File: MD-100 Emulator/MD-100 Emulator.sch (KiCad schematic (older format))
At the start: 12 parts

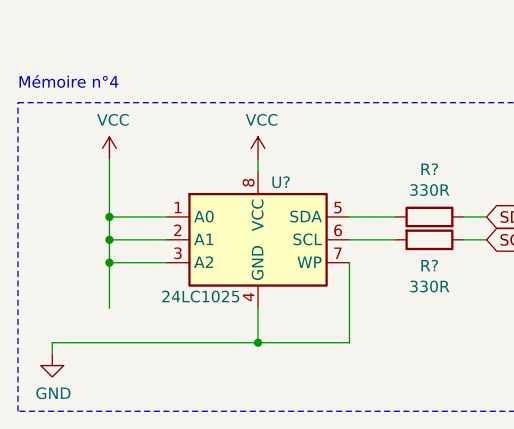
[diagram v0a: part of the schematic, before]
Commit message: j'ai enlevé un bout de ficelle qui gênait
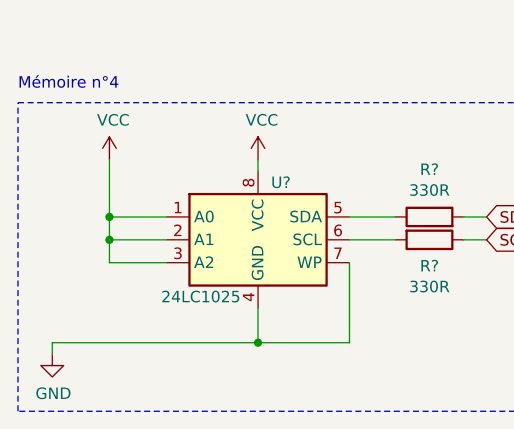
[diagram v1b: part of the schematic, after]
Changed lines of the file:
@@
 Wire Wire Line
 	1250 6800 1000 6800
-Connection ~ 1000 6800
-Wire Wire Line
-	1000 6800 1000 7000
 Wire Wire Line
 	1250 6700 1000 6700

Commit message: cours pcb alexx08
merci max de me le rappeller
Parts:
- added J?: CPB_Connector, symbol CoursPCB:CPB_Connector
- added U? (x5): 74HC00, symbol 74xx:74HC00
- added U? (x5): 74HC02, symbol 74xx:74HC02
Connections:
- wire segments 64 -> 103
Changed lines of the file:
@@
 Wire Wire Line
 	1250 1200 1000 1200
+$Comp
+L 74xx:74HC00 U?
+U 1 1 5EBDC272
+P 5000 4200
+F 0 "U?" H 5000 3883 50  0000 C CNN
+F 1 "74HC00" H 5000 3974 50  0000 C CNN
+F 2 "" H 5000 4200 50  0001 C CNN
+F 3 "http://www.ti.com/lit/gpn/sn74hc00" H 5000 4200 50  0001 C CNN
+	1    5000 4200
+	-1   0    0    1
+$EndComp
+$Comp
+L 74xx:74HC00 U?
+U 2 1 5EBE2FB7
+P 5000 5350
+F 0 "U?" H 5000 5033 50  0000 C CNN
+F 1 "74HC00" H 5000 5124 50  0000 C CNN
+F 2 "" H 5000 5350 50  0001 C CNN
+F 3 "http://www.ti.com/lit/gpn/sn74hc00" H 5000 5350 50  0001 C CNN
+	2    5000 5350
+	-1   0    0    1
+$EndComp
+$Comp
+L 74xx:74HC00 U?
+U 3 1 5EBE8E3D
+P 5750 5650
+F 0 "U?" H 5750 5333 50  0000 C CNN
+F 1 "74HC00" H 5750 5424 50  0000 C CNN
+F 2 "" H 5750 5650 50  0001 C CNN
+F 3 "http://www.ti.com/lit/gpn/sn74hc00" H 5750 5650 50  0001 C CNN
+	3    5750 5650
+	-1   0    0    1
+$EndComp
+$Comp
+L 74xx:74HC00 U?
+U 4 1 5EBEC491
+P 6550 5650
+F 0 "U?" H 6550 5333 50  0000 C CNN
+F 1 "74HC00" H 6550 5424 50  0000 C CNN
+F 2 "" H 6550 5650 50  0001 C CNN
+F 3 "http://www.ti.com/lit/gpn/sn74hc00" H 6550 5650 50  0001 C CNN
+	4    6550 5650
+	-1   0    0    1
+$EndComp
+$Comp
+L 74xx:74HC00 U?
+U 5 1 5EBEE381
+P 3700 6800
+F 0 "U?" H 3930 6846 50  0000 L CNN
+F 1 "74HC00" H 3930 6755 50  0000 L CNN
+F 2 "" H 3700 6800 50  0001 C CNN
+F 3 "http://www.ti.com/lit/gpn/sn74hc00" H 3700 6800 50  0001 C CNN
+	5    3700 6800
+	1    0    0    -1
+$EndComp
+Wire Wire Line
+	5300 5450 5400 5450
+Wire Wire Line
+	5400 5450 5400 5650
+Wire Wire Line
+	5400 5650 5450 5650
+Wire Wire Line
+	6050 5550 6150 5550
+Wire Wire Line
+	6050 5750 6150 5750
+Wire Wire Line
+	6150 5550 6150 5650
+Wire Wire Line
+	6150 5650 6250 5650
+Connection ~ 6150 5650
+Wire Wire Line
+	6150 5650 6150 5750
+Wire Wire Line
+	4700 5350 4400 5350
+Wire Wire Line
+	4400 5350 4400 4450
+Wire Wire Line
+	4700 4200 4400 4200
+$Comp
+L 74xx:74HC02 U?
+U 2 1 5EC153C3
+P 5750 3950
+F 0 "U?" H 5750 3633 50  0000 C CNN
+F 1 "74HC02" H 5750 3724 50  0000 C CNN
+F 2 "" H 5750 3950 50  0001 C CNN
+F 3 "http://www.ti.com/lit/gpn/sn74hc02" H 5750 3950 50  0001 C CNN
+	2    5750 3950
+	-1   0    0    1
+$EndComp
+$Comp
+L 74xx:74HC02 U?
+U 1 1 5EC1C40E
+P 5750 4500
+F 0 "U?" H 5750 4183 50  0000 C CNN
+F 1 "74HC02" H 5750 4274 50  0000 C CNN
+F 2 "" H 5750 4500 50  0001 C CNN
+F 3 "http://www.ti.com/lit/gpn/sn74hc02" H 5750 4500 50  0001 C CNN
+	1    5750 4500
+	-1   0    0    1
+$EndComp
+$Comp
+L 74xx:74HC02 U?
+U 4 1 5EC20EBA
+P 5750 5050
+F 0 "U?" H 5750 4733 50  0000 C CNN
+F 1 "74HC02" H 5750 4824 50  0000 C CNN
+F 2 "" H 5750 5050 50  0001 C CNN
+F 3 "http://www.ti.com/lit/gpn/sn74hc02" H 5750 5050 50  0001 C CNN
+	4    5750 5050
+	-1   0    0    1
+$EndComp
+$Comp
+L 74xx:74HC02 U?
+U 3 1 5EC2C9B1
+P 6600 3850
+F 0 "U?" H 6600 3533 50  0000 C CNN
+F 1 "74HC02" H 6600 3624 50  0000 C CNN
+F 2 "" H 6600 3850 50  0001 C CNN
+F 3 "http://www.ti.com/lit/gpn/sn74hc02" H 6600 3850 50  0001 C CNN
+	3    6600 3850
+	-1   0    0    1
+$EndComp
+$Comp
+L 74xx:74HC02 U?
+U 5 1 5EC31329
+P 4750 6800
+F 0 "U?" H 4980 6846 50  0000 L CNN
+F 1 "74HC02" H 4980 6755 50  0000 L CNN
+F 2 "" H 4750 6800 50  0001 C CNN
+F 3 "http://www.ti.com/lit/gpn/sn74hc02" H 4750 6800 50  0001 C CNN
+	5    4750 6800
+	1    0    0    -1
+$EndComp
+Wire Wire Line
+	5300 5250 5400 5250
+Wire Wire Line
+	5400 5250 5400 5050
+Wire Wire Line
+	5400 5050 5450 5050
+Wire Wire Line
+	5300 4300 5400 4300
+Wire Wire Line
+	5400 4300 5400 4500
+Wire Wire Line
+	5400 4500 5450 4500
+Wire Wire Line
+	5300 4100 5400 4100
+Wire Wire Line
+	5400 4100 5400 3950
+Wire Wire Line
+	5400 3950 5450 3950
+Wire Wire Line
+	6050 3850 6300 3850
+Wire Wire Line
+	6900 3750 7000 3750
+Wire Wire Line
+	7000 3750 7000 3950
+Wire Wire Line
+	6900 3950 7000 3950
+Wire Wire Line
+	6050 4950 7000 4950
+Wire Wire Line
+	6050 5150 8300 5150
+Wire Wire Line
+	7000 3950 7000 4950
+Connection ~ 7000 3950
+Connection ~ 7000 4950
+Wire Wire Line
+	7000 4950 8300 4950
+Wire Wire Line
+	6850 5550 7100 5550
+Wire Wire Line
+	6850 5750 7200 5750
+Wire Wire Line
+	7200 5750 7200 4400
+Wire Wire Line
+	7200 4400 6050 4400
+Wire Wire Line
+	6050 4600 7100 4600
+Wire Wire Line
+	7100 4600 7100 5550
+Wire Wire Line
+	7100 5550 8300 5550
+Connection ~ 7100 5550
+Wire Wire Line
+	7200 4400 7200 3300
+Connection ~ 7200 4400
+Wire Wire Line
+	6050 4050 7250 4050
+Wire Wire Line
+	7250 4050 7250 4850
+Wire Wire Line
+	7250 4850 8300 4850
+$Comp
+L CoursPCB:CPB_Connector J?
+U 1 1 5ECAD4C5
+P 9500 3000
+F 0 "J?" H 9475 3965 50  0000 C CNN
+F 1 "CPB_Connector" H 9475 3874 50  0000 C CNN
+F 2 "" H 9300 3850 50  0001 C CNN
+F 3 "" H 9300 3850 50  0001 C CNN
+	1    9500 3000
+	1    0    0    -1
+$EndComp
 $EndSCHEMATC

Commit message: Temp save
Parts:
- removed J?: CPB_Connector, symbol CoursPCB:CPB_Connector
- added C?: 10nF, symbol Device:C
- added C?: .1uF, symbol Device:C
- added C? (x2): 15pF, symbol Device:C_Small
- added D?: GRN, symbol Device:LED_Small
- added J1: CPB_Connector, symbol CoursPCB:CPB_Connector
- added R? (x3): R_Small, symbol Device:R_Small
- added R?: 330R, symbol Device:R
- added R? (x2): 10K, symbol Device:R_Small
- added U7: PIC18F452-IPT, Package_QFP:TQFP-44_10x10mm_P0.8mm, symbol MCU_Microchip_PIC18:PIC18F452-IPT
- added Y?: 4MHz, symbol Device:Crystal_Small
- gave numbers to parts that had none: 14
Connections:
- wire segments 103 -> 134
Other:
- moved on the sheet: U5A, U5B, U5C, U5D, U5E, U6A, U6B, U6C, U6D, U6E

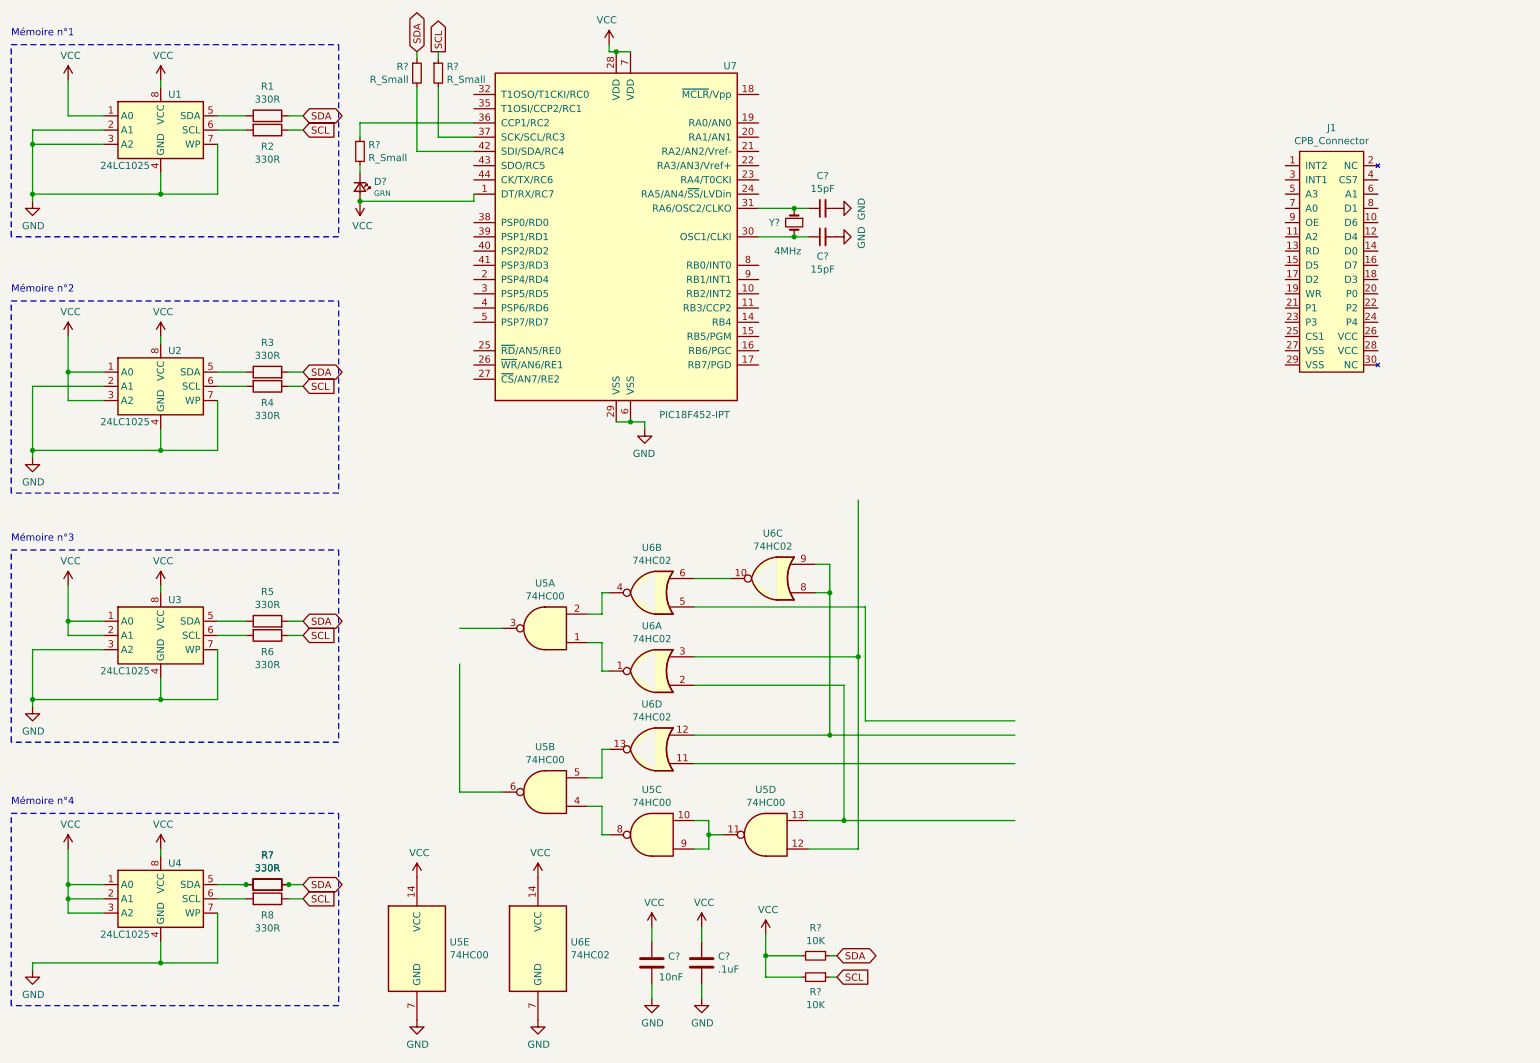
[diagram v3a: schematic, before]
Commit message: Added Pic + Bus + quartz
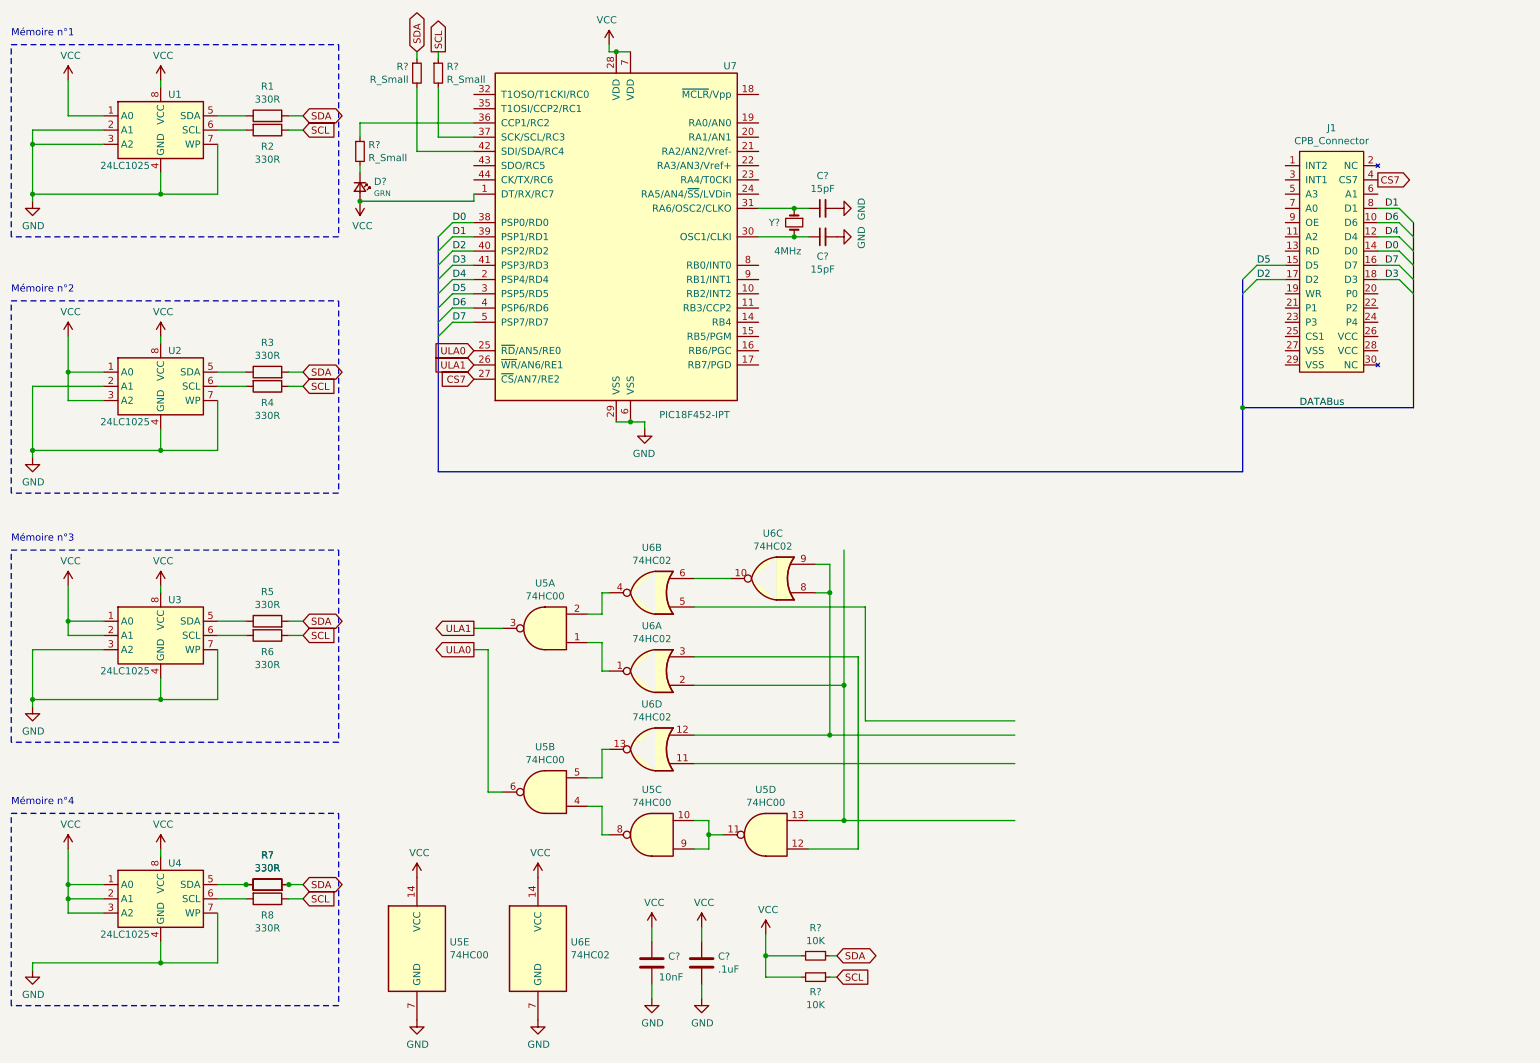
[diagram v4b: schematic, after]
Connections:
- net labels added: CS7, D0, D1, D2, D3, D4, D5, D6, D7, DATABus, ULA0, ULA1
- wire segments 134 -> 151
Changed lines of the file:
@@
 Wire Wire Line
 	5500 6250 5500 6350
-Wire Wire Line
-	4050 5950 3750 5950
-Wire Wire Line
-	3750 5950 3750 5050
-Wire Wire Line
-	4050 4800 3750 4800
 $Comp
 L 74xx:74HC02 U6
@@
 	6450 6150 7650 6150
 Connection ~ 6450 6150
-Wire Wire Line
-	6550 5000 6550 3900
-Connection ~ 6550 5000
 Wire Wire Line
 	5400 4650 6600 4650
@@
 	1    0    0    -1
 $EndComp
+Wire Wire Line
+	4050 4800 3850 4800
+Wire Wire Line
+	4050 5950 3950 5950
+Wire Wire Line
+	3950 5950 3950 4950
+Wire Wire Line
+	3950 4950 3850 4950
+Text GLabel 3850 4950 0    50   Output ~ 0
+ULA0
+Text GLabel 3850 4800 0    50   Output ~ 0
+ULA1
+Text GLabel 3850 2850 0    50   Input ~ 0
+ULA0
+Text GLabel 3850 2950 0    50   Input ~ 0
+ULA1
+Text GLabel 10200 1650 2    50   Output ~ 0
+CS7
+Text GLabel 3850 3050 0    50   Input ~ 0
+CS7
+Wire Wire Line
+	6450 5200 6450 4250
+Connection ~ 6450 5200
+Wire Wire Line
+	10200 2150 10350 2150
+Wire Wire Line
+	10200 2050 10350 2050
+Wire Wire Line
+	10200 1950 10350 1950
+Wire Wire Line
+	10200 1850 10350 1850
+Wire Wire Line
+	10200 2250 10350 2250
+Wire Wire Line
+	10200 2350 10350 2350
+Wire Wire Line
+	9550 2350 9350 2350
+Wire Wire Line
+	9550 2250 9350 2250
+Entry Wire Line
+	9350 2250 9250 2350
+Entry Wire Line
+	9350 2350 9250 2450
+Entry Wire Line
+	10350 2350 10450 2450
+Entry Wire Line
+	10350 2250 10450 2350
+Entry Wire Line
+	10350 2150 10450 2250
+Entry Wire Line
+	10350 2050 10450 2150
+Entry Wire Line
+	10350 1950 10450 2050
+Entry Wire Line
+	10350 1850 10450 1950
+Wire Wire Line
+	3850 1950 3700 1950
+Wire Wire Line
+	3850 2050 3700 2050
+Wire Wire Line
+	3850 2150 3700 2150
+Wire Wire Line
+	3850 2250 3700 2250
+Wire Wire Line
+	3850 2350 3700 2350
+Wire Wire Line
+	3850 2450 3700 2450
+Wire Wire Line
+	3850 2550 3700 2550
+Wire Wire Line
+	3850 2650 3700 2650
+Entry Wire Line
+	3700 1950 3600 2050
+Entry Wire Line
+	3700 2050 3600 2150
+Entry Wire Line
+	3700 2150 3600 2250
+Entry Wire Line
+	3700 2250 3600 2350
+Entry Wire Line
+	3700 2350 3600 2450
+Entry Wire Line
+	3700 2450 3600 2550
+Entry Wire Line
+	3700 2550 3600 2650
+Entry Wire Line
+	3700 2650 3600 2750
+Wire Bus Line
+	10450 3250 9250 3250
+Wire Bus Line
+	3600 3700 9250 3700
+Wire Bus Line
+	9250 3700 9250 3250
+Wire Bus Line
+	9250 2350 9250 3250
+Wire Bus Line
+	10450 1950 10450 3250
+Wire Bus Line
+	3600 2050 3600 3700
+Connection ~ 9250 3250
+Text Label 10250 2150 0    50   ~ 0
+D0
+Text Label 10250 2050 0    50   ~ 0
+D4
+Text Label 10250 1950 0    50   ~ 0
+D6
+Text Label 10250 1850 0    50   ~ 0
+D1
+Text Label 10250 2250 0    50   ~ 0
+D7
+Text Label 10250 2350 0    50   ~ 0
+D3
+Text Label 9350 2350 0    50   ~ 0
+D2
+Text Label 9350 2250 0    50   ~ 0
+D5
+Text Label 3700 1950 0    50   ~ 0
+D0
+Text Label 3700 2050 0    50   ~ 0
+D1
+Text Label 3700 2150 0    50   ~ 0
+D2
+Text Label 3700 2250 0    50   ~ 0
+D3
+Text Label 3700 2350 0    50   ~ 0
+D4
+Text Label 3700 2450 0    50   ~ 0
+D5
+Text Label 3700 2550 0    50   ~ 0
+D6
+Text Label 3700 2650 0    50   ~ 0
+D7
+Text Label 9650 3250 0    50   ~ 0
+DATABus
 $EndSCHEMATC

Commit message: MD-100 Terminé et annoté
à vérifier au minimum 1 fois encore
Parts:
- removed R?: 330R, symbol Device:R
- added C5: 15pF, symbol Device:C_Small
- added C6: 10uF, symbol Device:C_Small
- added C7: 0.1uF, symbol Device:C_Small
- added D2: BAV70, Package_TO_SOT_SMD:SOT-23, symbol Diode:BAV70
- added J2: I2CConn, symbol Connector:Conn_01x04_Male
- added J3: ICSP, symbol Connector:Conn_01x05_Male
- added Q1: NPN, symbol Device:Q_NPN_BEC
- added R12: 47K, symbol Device:R_Small
- added R16, R17, R19, R20: 100K, symbol Device:R_Small
- added R18: 220K, symbol Device:R
- added R21: 100k, symbol Device:R_Small
- added R9: 22K, symbol Device:R_Small
- R10: renamed from R?; value R_Small -> 4K7
- R11, R13: renamed from R?; value R_Small -> 330R
- gave numbers to parts that had none: 8
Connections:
- net labels added: A0, A1, A2, P0, P2, P3, P4, PGC, PGD, RD, WR, ~MCLR
- wire segments 151 -> 210
- no-connect marks 0 -> 18
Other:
- moved on the sheet: C1, C2, R14, R15, U5A, U5B, U5C, U5D, U5E, U6A, U6B, U6C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
